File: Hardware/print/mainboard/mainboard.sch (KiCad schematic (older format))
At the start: 14 parts

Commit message: Speisung angepasst, ohne Stückliste
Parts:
- removed C?: C10nF, symbol Device:C
- removed C?: 0.1uF, symbol Device:C
- removed C? (x2): 22uF, symbol Device:C
- removed L?: 2.2uH, symbol Device:L
- removed R?: 54.9k, symbol Device:R
- removed U?: LP2985A-33DBVR, Package_TO_SOT_SMD:SOT-23-5, symbol Regulator_Linear:LP2985-3.3
- removed U?: TPS565208DDCR, Package_TO_SOT_SMD:SOT-23-6, symbol Regulator_Switching:TPS562200
- added C? (x2): 10uF, symbol Device:C
- added C? (x2): 330uF, symbol Device:C
- added R?: 5.62k, symbol Device:R
- added R?: 42.2k, symbol Device:R
- added R?: 12.7k, symbol Device:R
- added U?: TLV70233_SOT23-5, Package_TO_SOT_SMD:SOT-23-5, symbol Regulator_Linear:TLV70233_SOT23-5
- added U?: LMZ12008TZE, symbol mylib:LMZ12008TZE
- C?: value 2.2uF -> 1uF
- C?: value 0.1uF -> 0.47uF
- R?: value 10k -> 1.07k
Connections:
- net 14V4: now also C?.1, C?.1, R?.1, U?.1 (VIN), U?.2 (VIN); no longer C?.1
- net GND: now also C?.2, C?.2, C?.2, C?.2, R?.2, U?.2 (GND), U?.3 (AGND), U?.5 (AGND), U?.6 (AGND), U?.~ (PGND)
- net at R?.1: now also R?.2, U?.7 (FB)
- net 3V3 renamed +3V3
- net +3V3: now also U?.5 (OUT)
- net 5V renamed +5V
- net +5V: now also C?.1, C?.1, R?.1, U?.1 (IN), U?.10 (VOUT), U?.11 (VOUT), U?.3 (EN)
- new net: C?.1, U?.8 (SSC)
- new net: R?.1, R?.2, U?.4 (EN)
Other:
- moved on the sheet: C?, R?

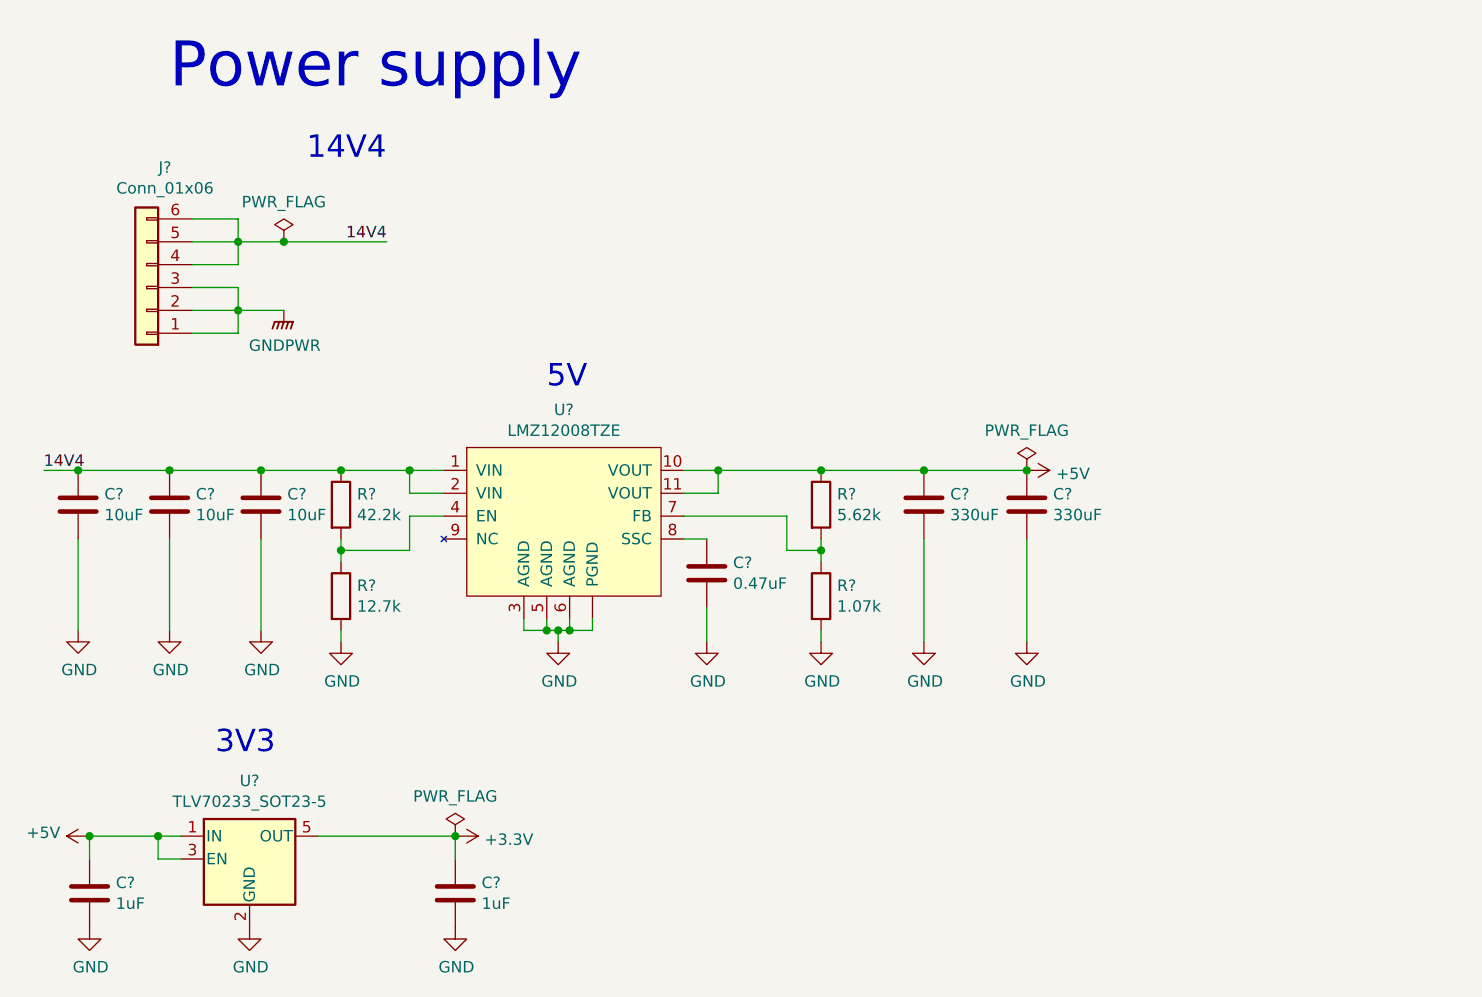
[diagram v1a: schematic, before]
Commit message: Stückliste aktualisiert (Speisung)
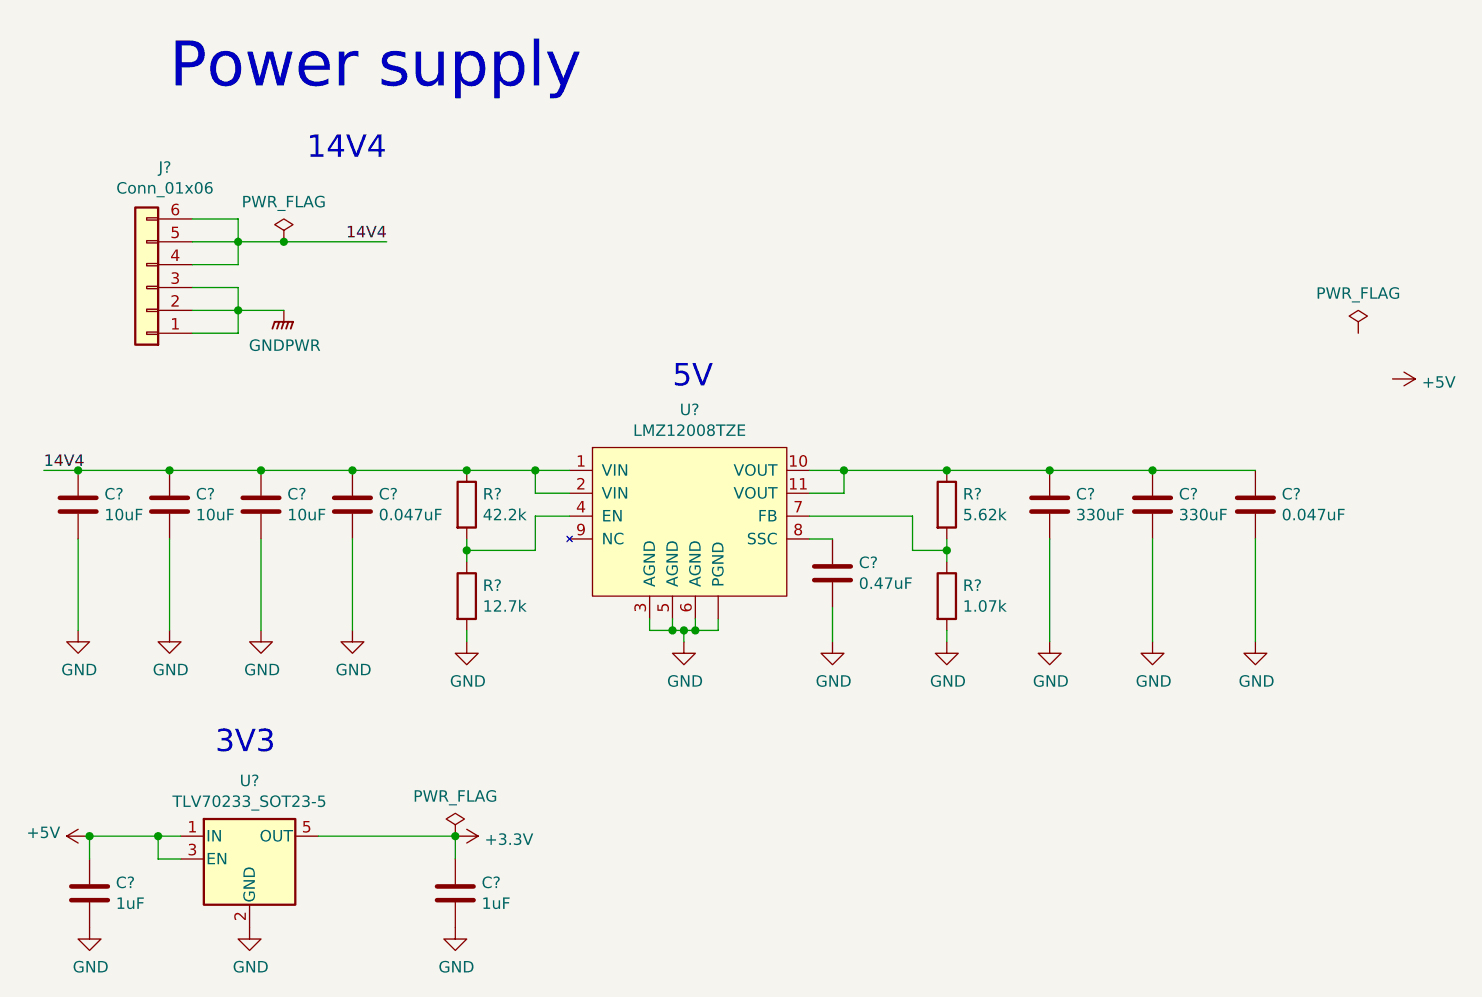
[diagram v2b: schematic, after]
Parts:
- added C? (x2): 0.047uF, symbol Device:C
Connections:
- net +5V: no longer C?.1, C?.1, R?.1, U?.10 (VOUT), U?.11 (VOUT)
- net 14V4: now also C?.1
- net GND: now also C?.2, C?.2
- new net: C?.1, C?.1, C?.1, R?.1, U?.10 (VOUT), U?.11 (VOUT)
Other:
- moved on the sheet: C?, R?, U?

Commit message: Pflichtenheft Speisung ergänzt
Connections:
- net +5V: now also C?.1, C?.1, C?.1, R?.1, U?.10 (VOUT), U?.11 (VOUT)
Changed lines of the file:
@@
 L power:PWR_FLAG #FLG?
 U 1 1 5E639DC6
-P 6600 1850
-F 0 "#FLG?" H 6600 1925 50  0001 C CNN
-F 1 "PWR_FLAG" H 6600 2024 50  0000 C CNN
-F 2 "" H 6600 1850 50  0001 C CNN
-F 3 "~" H 6600 1850 50  0001 C CNN
-	1    6600 1850
+P 5900 2450
+F 0 "#FLG?" H 5900 2525 50  0001 C CNN
+F 1 "PWR_FLAG" H 5900 2624 50  0000 C CNN
+F 2 "" H 5900 2450 50  0001 C CNN
+F 3 "~" H 5900 2450 50  0001 C CNN
+	1    5900 2450
 	1    0    0    -1
 $EndComp
@@
 L power:+5V #PWR?
 U 1 1 5E6CFB15
-P 6750 2050
-F 0 "#PWR?" H 6750 1900 50  0001 C CNN
-F 1 "+5V" V 6765 2178 50  0000 L CNN
-F 2 "" H 6750 2050 50  0001 C CNN
-F 3 "" H 6750 2050 50  0001 C CNN
-	1    6750 2050
+P 6150 2450
+F 0 "#PWR?" H 6150 2300 50  0001 C CNN
+F 1 "+5V" V 6165 2578 50  0000 L CNN
+F 2 "" H 6150 2450 50  0001 C CNN
+F 3 "" H 6150 2450 50  0001 C CNN
+	1    6150 2450
 	0    1    1    0
 $EndComp
@@
 $EndComp
 Wire Wire Line
-	6150 2450 5700 2450
+	6150 2450 5900 2450
 Connection ~ 5700 2450
 Wire Wire Line
 	6150 2750 6150 3200
+Connection ~ 5900 2450
+Wire Wire Line
+	5900 2450 5700 2450
+Connection ~ 6150 2450
 $EndSCHEMATC
